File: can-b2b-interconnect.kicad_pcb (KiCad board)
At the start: 2 copper layers, 10.3 x 11.8 mm, 4 parts, among them J2 USB4110GFA, U1 DF52-4S-0.8H(21)

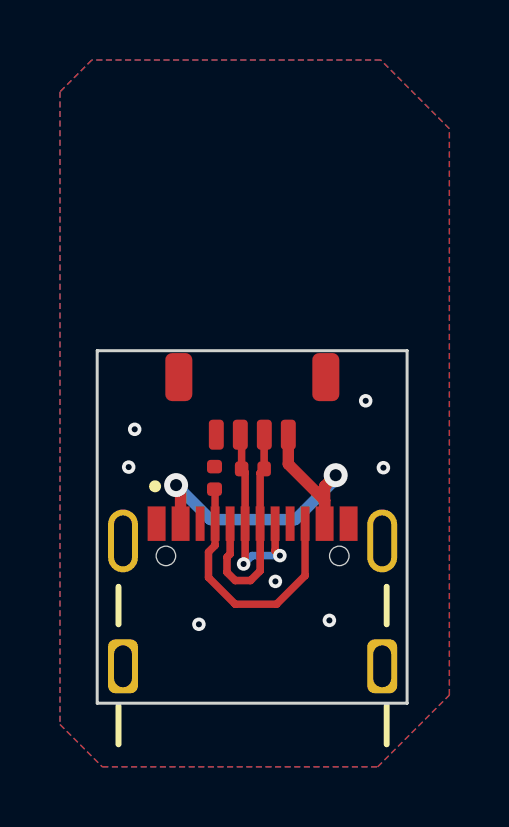
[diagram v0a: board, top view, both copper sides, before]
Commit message: fix clearance issue
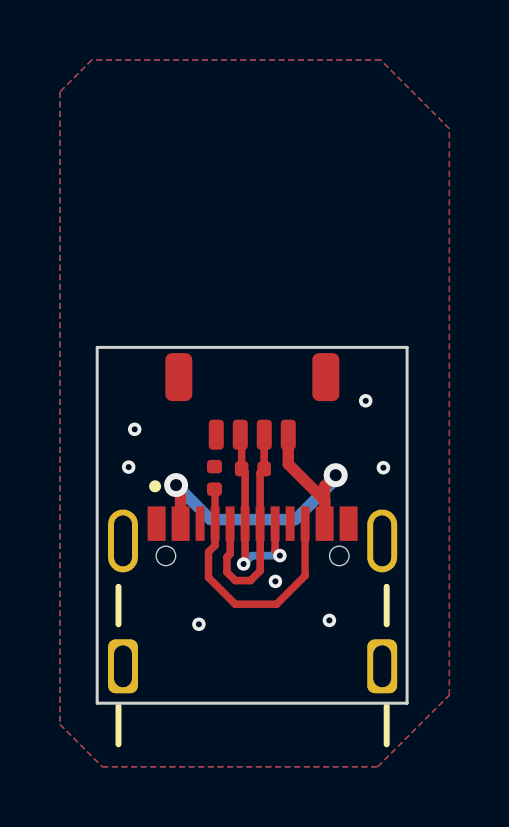
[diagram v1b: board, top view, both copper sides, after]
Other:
- board size 10.3 x 11.8 mm -> 10.3 x 11.9 mm
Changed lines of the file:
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@@
     )
   )
-  (gr_rect (start 97.92 63.25) (end 108.25 75)
+  (gr_rect (start 97.92 63.14) (end 108.25 75)
     (stroke (width 0.1) (type default)) (fill none) (layer "Edge.Cuts"))
   (segment (start 100.7 67.88) (end 100.55 67.73) (width 0.381) (layer "F.Cu") (net 1))
